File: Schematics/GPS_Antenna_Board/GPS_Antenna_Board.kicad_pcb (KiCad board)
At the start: 2 copper layers, 50 x 65 mm, 31 parts, among them J2 SATA Conn. (Male), U1 SAM-M10Q

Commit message: Add JLCJLC silkscreen text
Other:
- board text added: "JLCJLCJLCJLC"
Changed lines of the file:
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@@
     (effects (font (size 0.8 0.8) (thickness 0.15) bold) (justify left bottom mirror))
+  )
+  (gr_text "JLCJLCJLCJLC" (at 147.7 137) (layer "B.SilkS")
+    (effects (font (size 1 1) (thickness 0.15)) (justify top mirror))
   )
   (gr_text "RESET" (at 146.5 133.9) (layer "B.SilkS")

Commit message: Bump revision number to V2.0 & V1.2
GPS module is V2.0, Antenna PCB is V1.2
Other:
- board text added: "Gouda Rev 1.2 QRET Feb 2025 Tristan Alderson Kennan Bays"
- board text removed: "Gouda Rev 1.1 QRET May 2024 Tristan Alderson Kennan Bays"
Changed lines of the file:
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@@
   (gr_arc (start 171 74.2) (mid 172.202082 74.697918) (end 172.7 75.9)
     (stroke (width 0.1) (type default)) (layer "Edge.Cuts"))
-  (gr_text "Gouda Rev 1.1\nQRET May 2024\n\nTristan Alderson\nKennan Bays" (at 147.7 85.35) (layer "B.SilkS")
+  (gr_text "Gouda Rev 1.2\nQRET Feb 2025\n\nTristan Alderson\nKennan Bays" (at 147.7 85.35) (layer "B.SilkS")
     (effects (font (size 1.5 1.5) (thickness 0.25)) (justify top mirror))
   )

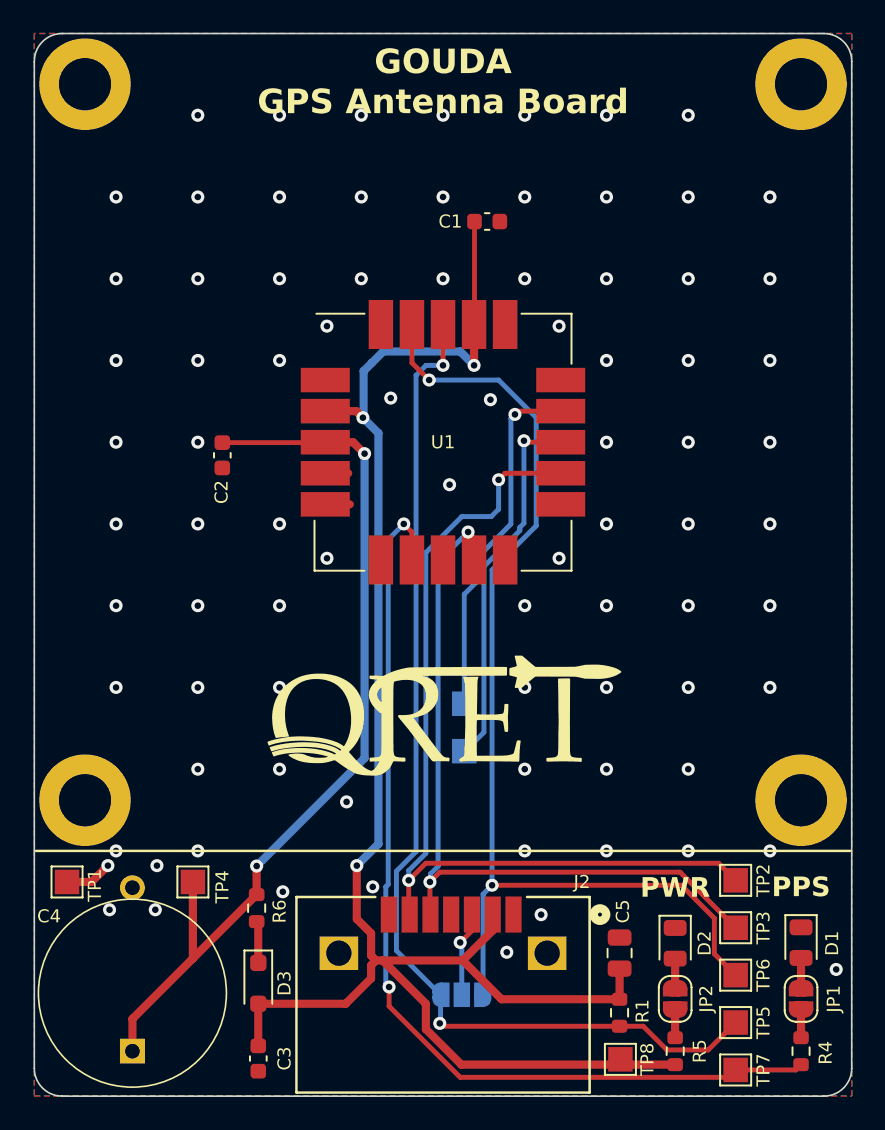
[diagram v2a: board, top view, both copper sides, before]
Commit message: Revised PCB layout of GPS Antenna PCB
The main change was adding the new connector, as well as re-arranging the TX/RX breakout pads
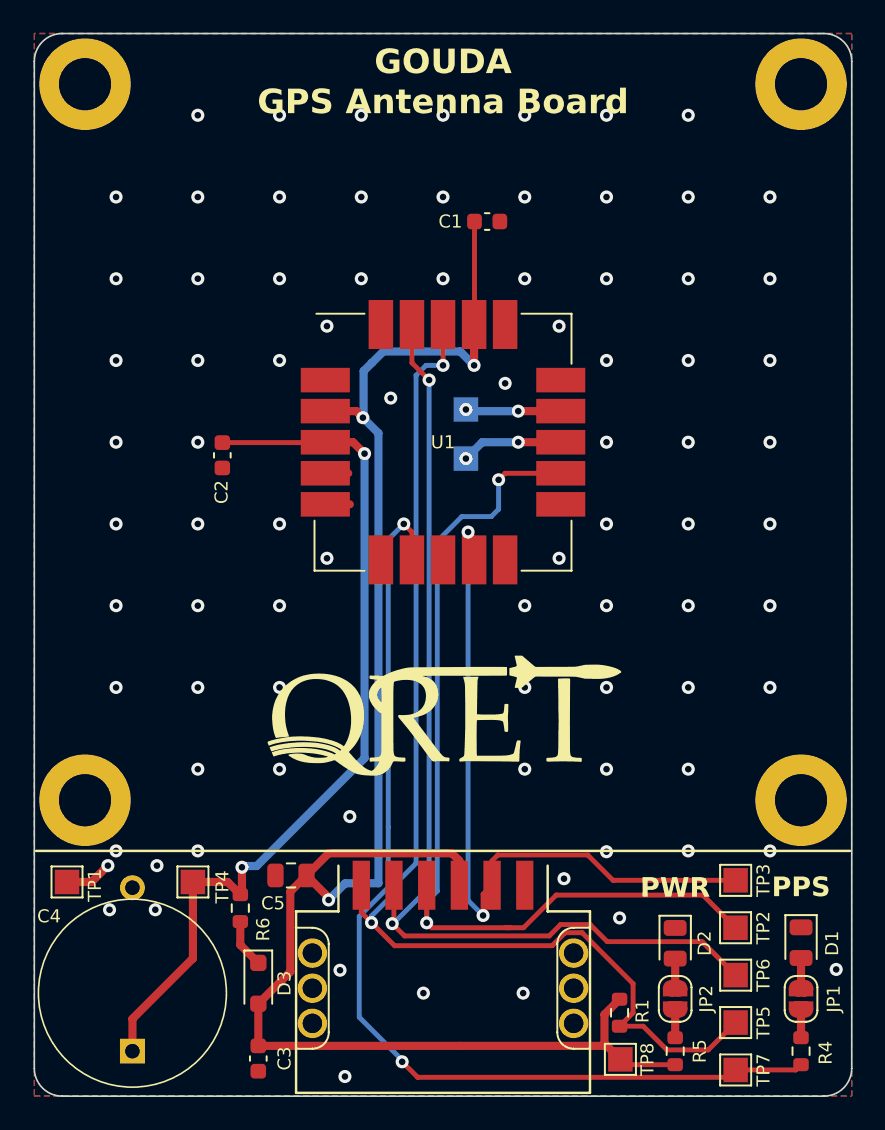
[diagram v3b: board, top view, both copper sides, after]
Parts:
- removed J2: SATA Conn. (Male), footprints:CONN_47080-4001_MOL_SATA
- removed JP3: P3 FUNC, Jumper:SolderJumper-3_P1.3mm_Open_RoundedPad1.0x1.5mm
- added J1: GT8E-6P-2H(55), footprints:CONN_GT8E-6P-2H(55), F.Cu at (147.7, 132.1)
- moved C5 20.7 mm to (138.4, 125.7), turned to 0 degrees
- moved TP9 18.0 mm to (149.1, 97.2)
- moved TP10 17.9 mm to (149.1, 100.2)
- moved TP2 2.90 mm to (165.6, 128.9)
- moved TP3 2.90 mm to (165.6, 126.0)
- moved R6 1.00 mm to (135.3, 127.7)
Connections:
- C5 pad 1: +3.3V -> GND
- C5 pad 2: GND -> +3.3V
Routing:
- net Net-(U1-TXD): track 22.8 -> 6.21 mm, vias 1 -> 2
- net Net-(U1-RXD): track 21.9 -> 5.84 mm, vias 1 -> 2
- net GPS_RST: track 65.1 -> 71.1 mm
- net Net-(JP3-C): track 5.24 -> 0.00 mm, vias 1 -> 0
- net GPS_EXTINT: track 66.4 -> 63.3 mm
- net GPS_PPS: track 59.8 -> 62.6 mm
- net SCL: track 54.8 -> 57.2 mm
- net +3.3V: track 110.5 -> 108.7 mm
- net SDA: track 46.6 -> 45.0 mm
- net BCKP_BATT: track 56.3 -> 54.9 mm
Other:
- board text removed: "EXTINT"
- board text removed: "JLCJLCJLCJLC"
- board text removed: "P3 USE"
- board text removed: "RESET"

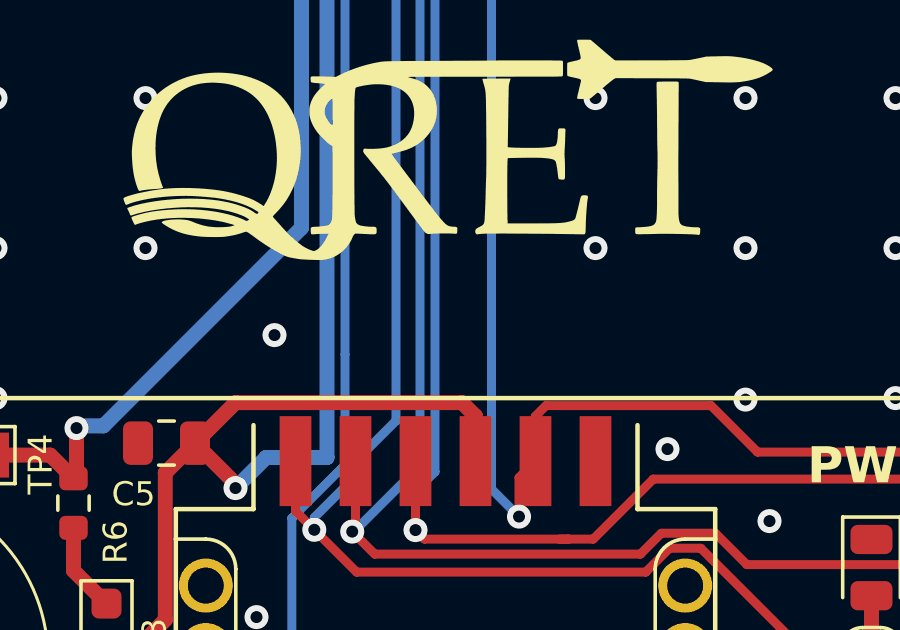
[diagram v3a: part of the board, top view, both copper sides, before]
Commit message: Added "PB-FREE" silkscreen to GPS antenna PCB
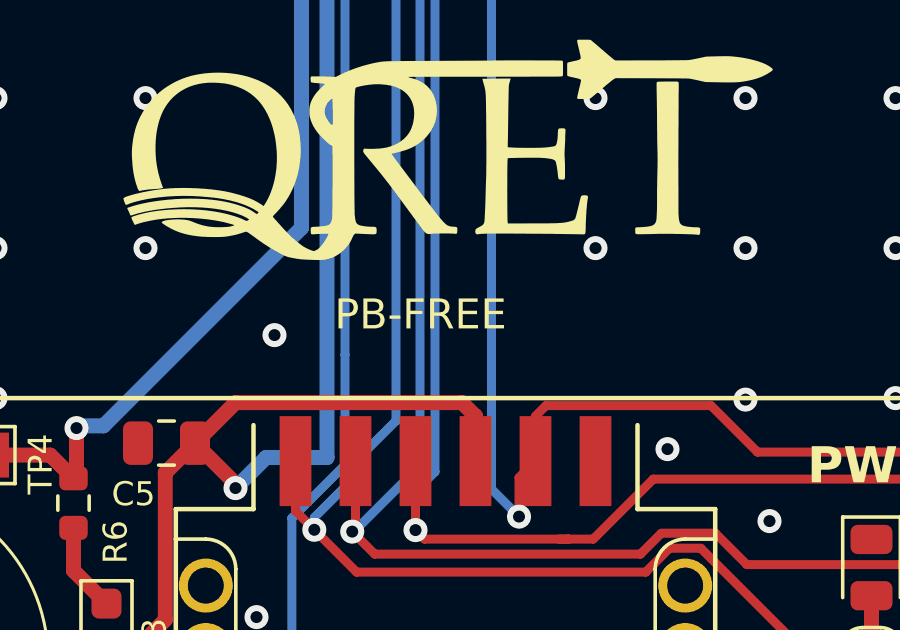
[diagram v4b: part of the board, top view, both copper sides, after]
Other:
- board text added: "PB-FREE"
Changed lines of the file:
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@@
     (effects (font (size 0.9 0.9) (thickness 0.18) bold) (justify mirror))
+  )
+  (gr_text "PB-FREE" (at 151 117) (layer "B.SilkS")
+    (effects (font (size 1 1) (thickness 0.15)) (justify left bottom mirror))
   )
   (gr_text "TX" (at 146.5 100.1) (layer "B.SilkS")
@@
     (effects (font (size 1.2 1.2) (thickness 0.2) bold) (justify bottom))
   )
+  (gr_text "PB-FREE" (at 144 122) (layer "F.SilkS")
+    (effects (font (size 1 1) (thickness 0.15)) (justify left bottom))
+  )
   (gr_text "PPS" (at 169.6 127.1125) (layer "F.SilkS" knockout)

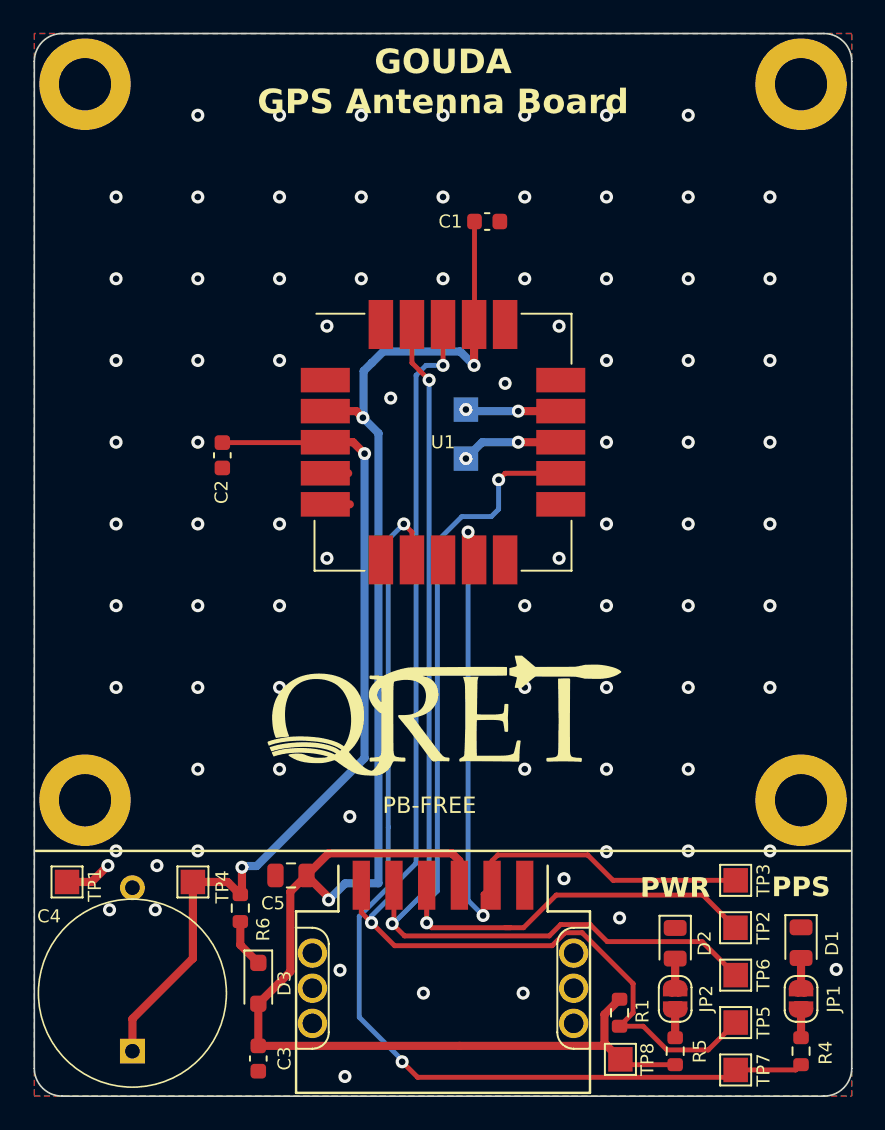
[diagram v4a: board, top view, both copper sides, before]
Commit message: Quick adjustments to Antenna PCB
- Added proper silkscreen labels to test points
- Added version number on front of PCB
- Updated version date
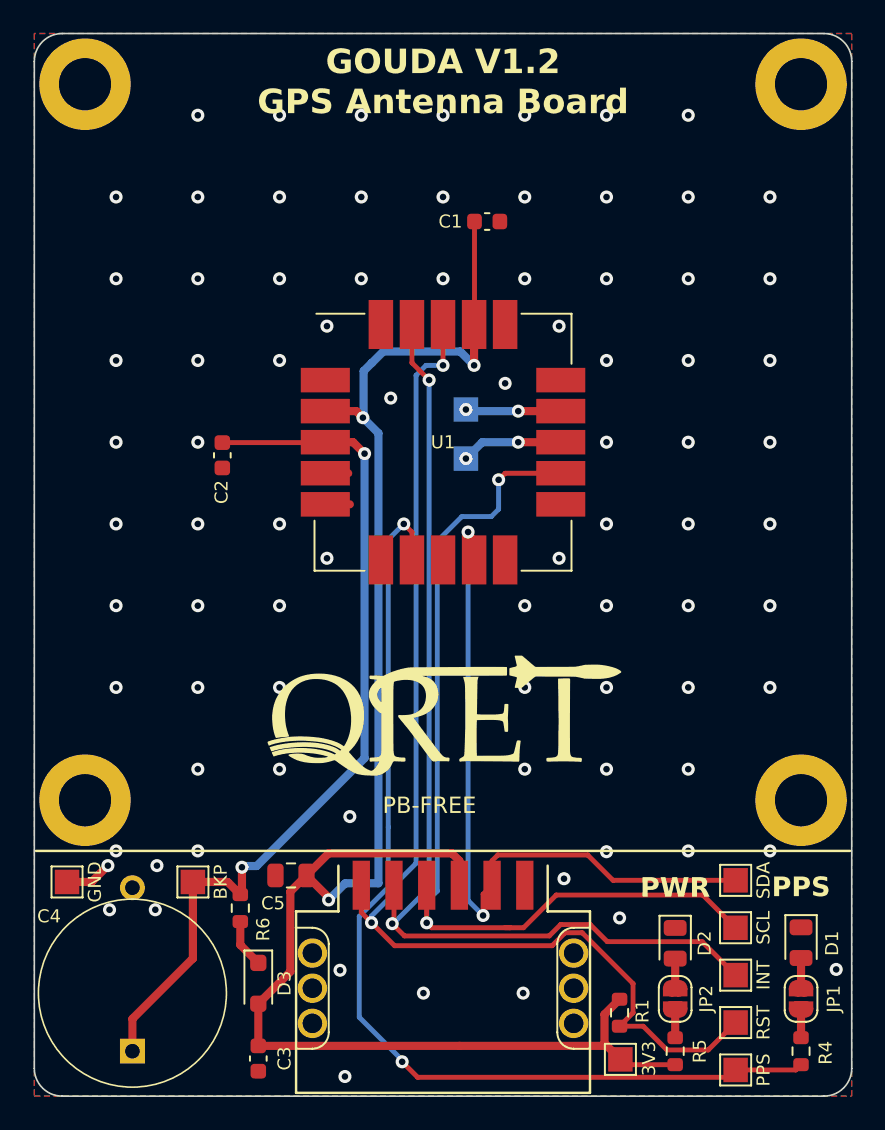
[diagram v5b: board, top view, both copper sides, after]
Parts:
- TP1: value TP_GND -> GND
- TP2: value TP_SCL -> SCL
- TP3: value TP_SDA -> SDA
- TP4: value TP_BCKP -> BKP
- TP5: value TP_RST -> RST
- TP6: value TP_INT -> INT
- TP7: value TP_PPS -> PPS
- TP8: value TP_3.3V -> 3V3
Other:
- board text added: "GOUDA V1.2"
- board text added: "Gouda Rev 1.2 QRET Mar 2025 Tristan Alderson Kennan Bays"
- board text removed: "GOUDA"
- board text removed: "Gouda Rev 1.2 QRET Feb 2025 Tristan Alderson Kennan Bays"
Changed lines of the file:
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@@
     (property "ki_keywords" "test point tp")
     (attr exclude_from_pos_files exclude_from_bom)
-    (fp_text reference "TP3" (at 1.7 0 90) (layer "F.SilkS")
+    (fp_text reference "TP3" (at 1.7 0 90) (layer "F.SilkS") hide
         (effects (font (size 0.8 0.8) (thickness 0.1)))
     )
-    (fp_text value "TP_SDA" (at 0.5 3.2) (layer "F.Fab")
-        (effects (font (size 1 1) (thickness 0.15)))
+    (fp_text value "SDA" (at 1.7 0 -90) (layer "F.SilkS")
+        (effects (font (size 0.8 0.8) (thickness 0.1)))
     )
     (fp_text user "${REFERENCE}" (at 0 -1.65) (layer "F.Fab")
@@
     (property "ki_keywords" "test point tp")
     (attr exclude_from_pos_files exclude_from_bom)
-    (fp_text reference "TP7" (at 1.7 0 90) (layer "F.SilkS")
+    (fp_text reference "TP7" (at 1.7 0 90) (layer "F.SilkS") hide
         (effects (font (size 0.8 0.8) (thickness 0.1)))
     )
-    (fp_text value "TP_PPS" (at 0 1.75) (layer "F.Fab")
-        (effects (font (size 1 1) (thickness 0.15)))
+    (fp_text value "PPS" (at 1.7 0 90) (layer "F.SilkS")
+        (effects (font (size 0.8 0.8) (thickness 0.1)))
     )
     (fp_text user "${REFERENCE}" (at 0 -1.65) (layer "F.Fab")
@@
     (property "ki_keywords" "test point tp")
     (attr exclude_from_pos_files exclude_from_bom)
-    (fp_text reference "TP8" (at 1.65 0 -90) (layer "F.SilkS")
+    (fp_text reference "TP8" (at 1.65 0 -90) (layer "F.SilkS") hide
         (effects (font (size 0.8 0.8) (thickness 0.1)))
     )
-    (fp_text value "TP_3.3V" (at 0 1.75) (layer "F.Fab")
-        (effects (font (size 1 1) (thickness 0.15)))
+    (fp_text value "3V3" (at 1.75 -0.05 90) (layer "F.SilkS")
+        (effects (font (size 0.8 0.8) (thickness 0.1)))
     )
     (fp_text user "${REFERENCE}" (at 0 -1.65) (layer "F.Fab")
@@
     (property "ki_keywords" "test point tp")
     (attr exclude_from_pos_files exclude_from_bom)
-    (fp_text reference "TP5" (at 1.7 0 90) (layer "F.SilkS")
+    (fp_text reference "TP5" (at 1.7 0 90) (layer "F.SilkS") hide
         (effects (font (size 0.8 0.8) (thickness 0.1)))
     )
-    (fp_text value "TP_RST" (at 0.5 3.2) (layer "F.Fab")
-        (effects (font (size 1 1) (thickness 0.15)))
+    (fp_text value "RST" (at 1.7 0 90) (layer "F.SilkS")
+        (effects (font (size 0.8 0.8) (thickness 0.1)))
     )
     (fp_text user "${REFERENCE}" (at 0 -1.65) (layer "F.Fab")
@@
     (property "ki_keywords" "test point tp")
     (attr exclude_from_pos_files exclude_from_bom)
-    (fp_text reference "TP2" (at 1.7 0 90) (layer "F.SilkS")
+    (fp_text reference "TP2" (at 1.7 0 90) (layer "F.SilkS") hide
         (effects (font (size 0.8 0.8) (thickness 0.1)))
     )
-    (fp_text value "TP_SCL" (at 0.5 3.2) (layer "F.Fab")
-        (effects (font (size 1 1) (thickness 0.15)))
+    (fp_text value "SCL" (at 1.707106 0 90) (layer "F.SilkS")
+        (effects (font (size 0.8 0.8) (thickness 0.1)))
     )
     (fp_text user "${REFERENCE}" (at 0 -1.65) (layer "F.Fab")
@@
     (property "ki_keywords" "test point tp")
     (attr exclude_from_pos_files exclude_from_bom)
-    (fp_text reference "TP4" (at 1.8 0.3 90) (layer "F.SilkS")
+    (fp_text reference "TP4" (at 1.8 0.3 90) (layer "F.SilkS") hide
         (effects (font (size 0.8 0.8) (thickness 0.1)))
     )
-    (fp_text value "TP_BCKP" (at 0 1.75) (layer "F.Fab")
-        (effects (font (size 1 1) (thickness 0.15)))
+    (fp_text value "BKP" (at 1.7 0 90) (layer "F.SilkS")
+        (effects (font (size 0.8 0.8) (thickness 0.1)))
     )
     (fp_text user "${REFERENCE}" (at 0 -1.65) (layer "F.Fab")
@@
     (property "ki_keywords" "test point tp")
     (attr exclude_from_pos_files exclude_from_bom)
-    (fp_text reference "TP1" (at 1.7 0.2 -90) (layer "F.SilkS")
+    (fp_text reference "TP1" (at 1.7 0.2 -90) (layer "F.SilkS") hide
         (effects (font (size 0.8 0.8) (thickness 0.1)))
     )
-    (fp_text value "TP_GND" (at 0 1.75) (layer "F.Fab")
-        (effects (font (size 1 1) (thickness 0.15)))
+    (fp_text value "GND" (at 1.7 0 -90) (layer "F.SilkS")
+        (effects (font (size 0.8 0.8) (thickness 0.1)))
     )
     (fp_text user "${REFERENCE}" (at 0 -1.65) (layer "F.Fab")
@@
     (property "ki_keywords" "test point tp")
     (attr exclude_from_pos_files exclude_from_bom)
-    (fp_text reference "TP6" (at 1.7 0 90) (layer "F.SilkS")
+    (fp_text reference "TP6" (at 1.7 0 90) (layer "F.SilkS") hide
         (effects (font (size 0.8 0.8) (thickness 0.1)))
     )
-    (fp_text value "TP_INT" (at 0 1.75) (layer "F.Fab")
-        (effects (font (size 1 1) (thickness 0.15)))
+    (fp_text value "INT" (at 1.7 0 90) (layer "F.SilkS")
+        (effects (font (size 0.8 0.8) (thickness 0.1)))
     )
     (fp_text user "${REFERENCE}" (at 0 -1.65) (layer "F.Fab")
@@
   (gr_arc (start 171 74.2) (mid 172.202082 74.697918) (end 172.7 75.9)
     (stroke (width 0.1) (type default)) (layer "Edge.Cuts"))
-  (gr_text "Gouda Rev 1.2\nQRET Feb 2025\n\nTristan Alderson\nKennan Bays" (at 147.7 79.6) (layer "B.SilkS")
+  (gr_text "Gouda Rev 1.2\nQRET Mar 2025\n\nTristan Alderson\nKennan Bays" (at 147.7 79.6) (layer "B.SilkS")
     (effects (font (size 1.5 1.5) (thickness 0.25)) (justify top mirror))
   )
@@
     (effects (font (size 1.5 1.5) (thickness 0.3) bold) (justify top))
   )
-  (gr_text "GOUDA" (at 147.7 75.05) (layer "F.SilkS" knockout)
+  (gr_text "GOUDA V1.2" (at 147.7 75.05) (layer "F.SilkS" knockout)
     (effects (font (size 1.5 1.5) (thickness 0.3) bold) (justify top))
   )

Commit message: Finalized silkscreen
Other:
- board text added: "GPS Antenna Board V1.2"
- board text added: "NASONOV Antenna"
- board text added: "NASONOV Antenna Rev 1.2 QRET Mar 2025 Tristan Alderson Kennan Bays"
- board text removed: "GOUDA V1.2"
- board text removed: "GPS Antenna Board"
- board text removed: "Gouda Rev 1.2 QRET Mar 2025 Tristan Alderson Kennan Bays"
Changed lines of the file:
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@@
       (psa4output false)
       (plotreference true)
-      (plotvalue false)
+      (plotvalue true)
       (plotinvisibletext false)
       (sketchpadsonfab false)
@@
   (gr_arc (start 171 74.2) (mid 172.202082 74.697918) (end 172.7 75.9)
     (stroke (width 0.1) (type default)) (layer "Edge.Cuts"))
-  (gr_text "Gouda Rev 1.2\nQRET Mar 2025\n\nTristan Alderson\nKennan Bays" (at 147.7 79.6) (layer "B.SilkS")
+  (gr_text "NASONOV Antenna Rev 1.2\nQRET Mar 2025\n\nTristan Alderson\nKennan Bays" (at 147.7 79.6) (layer "B.SilkS")
     (effects (font (size 1.5 1.5) (thickness 0.25)) (justify top mirror))
   )
@@
     (effects (font (size 0.9 0.9) (thickness 0.18) bold) (justify mirror))
   )
-  (gr_text "GPS Antenna Board" (at 147.7 77.5) (layer "F.SilkS" knockout)
+  (gr_text "GPS Antenna Board V1.2" (at 147.7 77.5) (layer "F.SilkS" knockout)
     (effects (font (size 1.5 1.5) (thickness 0.3) bold) (justify top))
   )
-  (gr_text "GOUDA V1.2" (at 147.7 75.05) (layer "F.SilkS" knockout)
+  (gr_text "NASONOV Antenna" (at 147.7 75.05) (layer "F.SilkS" knockout)
     (effects (font (size 1.5 1.5) (thickness 0.3) bold) (justify top))
   )
